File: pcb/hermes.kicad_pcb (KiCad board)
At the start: 2 copper layers, 28.5 x 68 mm, 17 parts, among them J1 OLED_128x64, U1 XIAO-RP2040-DIP, U2 MAX30102, U3 VL53L1CXV0FY1

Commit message: Added resistor in PCB
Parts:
- added R5: 4.7k, Resistor_SMD:R_0805_2012Metric, F.Cu at (144.6, 108.4)
- added R6: 4.7k, Resistor_SMD:R_0805_2012Metric, F.Cu at (147.5, 108.4)
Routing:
- net +3V3: track 86.0 -> 93.8 mm
- net SDA: track 47.6 -> 55.1 mm, vias 0 -> 1
- net SCL: track 37.3 -> 38.5 mm, vias 2 -> 3

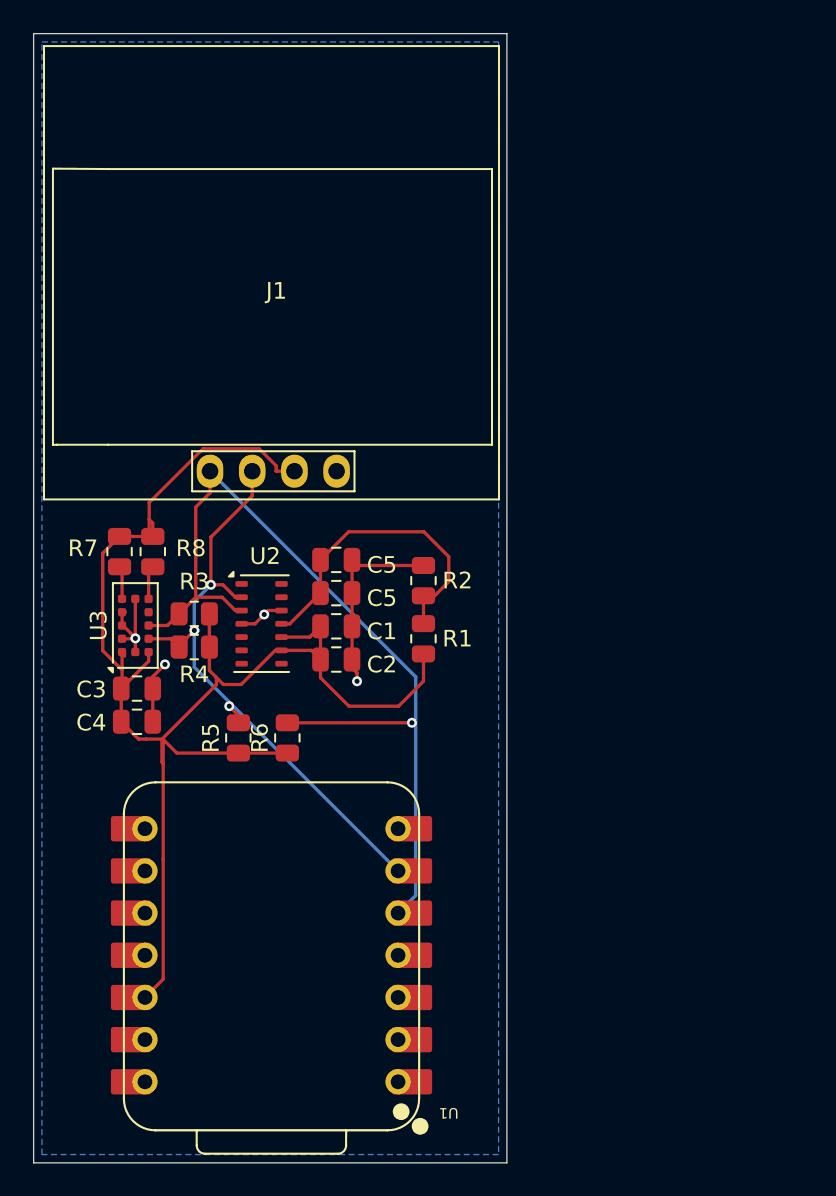
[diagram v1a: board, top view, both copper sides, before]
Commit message: Convert to ToF devboard (use previous versions for full Hermes board
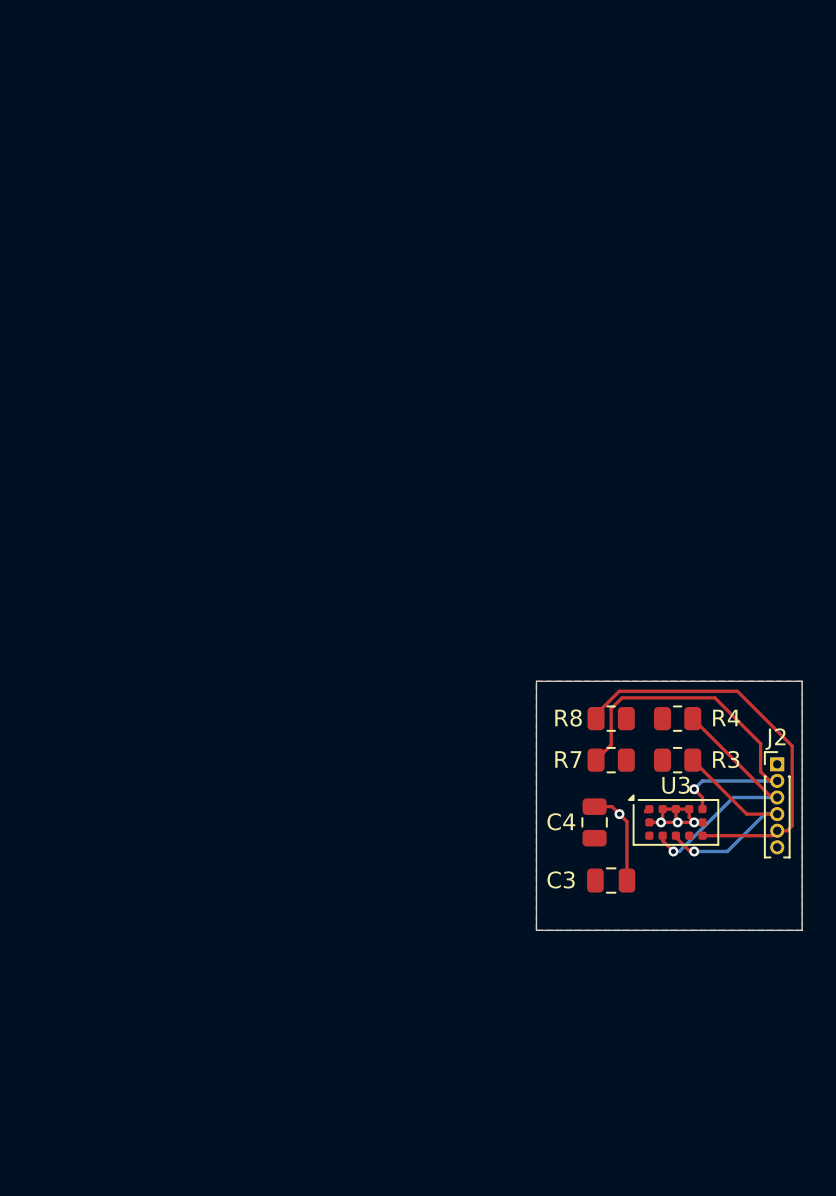
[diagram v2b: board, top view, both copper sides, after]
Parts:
- removed C1: 10u, Capacitor_SMD:C_0805_2012Metric
- removed C2, C6: 0.1u, Capacitor_SMD:C_0805_2012Metric
- removed C5: 4.7u, Capacitor_SMD:C_0805_2012Metric
- removed J1: OLED_128x64, SSD1306:128x64OLED
- removed R1: 1k, Resistor_SMD:R_0805_2012Metric
- removed R2: 2.2k, Resistor_SMD:R_0805_2012Metric
- removed R5, R6: 4.7k, Resistor_SMD:R_0805_2012Metric
- removed U1: XIAO-RP2040-DIP, EE Parts:XIAO-RP2040-DIP
- removed U2: MAX30102, OptoDevice:Maxim_OLGA-14_3.3x5.6mm_P0.8mm
- added J2: Conn_01x06_Pin, Connector_PinHeader_1.00mm:PinHeader_1x06_P1.00mm_Vertical, F.Cu at (177.0, 110.0)
- moved G*** 74.9 mm to (167.5, 110.0), turned to 180 degrees
- moved U3 34.6 mm to (170.9, 113.5), turned to 0 degrees
- moved R7 32.2 mm to (167.0, 109.8), turned to 180 degrees
- moved C3 30.8 mm to (167.0, 117.0)
- moved R3 30.4 mm to (171.0, 109.8), turned to 0 degrees
- moved R4 29.4 mm to (171.0, 107.2), turned to 0 degrees
- moved R8 29.4 mm to (167.0, 107.2), turned to 180 degrees
- moved C4 28.2 mm to (166.0, 113.5), turned to 90 degrees
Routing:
- net +3V3: track 93.8 -> 0.39 mm
- net SDA: track 55.1 -> 13.9 mm
- net SCL: track 38.5 -> 15.9 mm, vias 3 -> 1
- net TOF_INT: track 2.04 -> 24.5 mm
- net XSHUT: track 2.00 -> 23.4 mm, vias 0 -> 1
- net +1V8: track 19.4 -> 0.00 mm
- net GND: track 25.3 -> 13.3 mm
- added copper zone on F.Cu, net +3V3
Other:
- board size 28.5 x 68 mm -> 16 x 15 mm
- board text added: "+3V3"
- board text added: "GND"
- board text added: "INT"
- board text added: "SCL"
- board text added: "SDA"
- board text added: "VL53L1X TOF Breakout"
- board text added: "XSHUT"
- board text removed: "Aadarsh Heart Monitor (MAX30102) TOF Sensor (VL53L1X)"
- board text removed: "C5"
